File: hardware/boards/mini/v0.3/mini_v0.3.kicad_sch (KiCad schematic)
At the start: 96 parts, among them IC1 NAU88C22YG, IC3 IS42S16160J-6BLI, J1 Connector, J2 Top (A), J3 Bottom (B), U1 W25Q128JVP, U2 LTV-217-G, U4 STM32H750XBHx, Y1 Crystal_GND24, Y3 32.768kHz

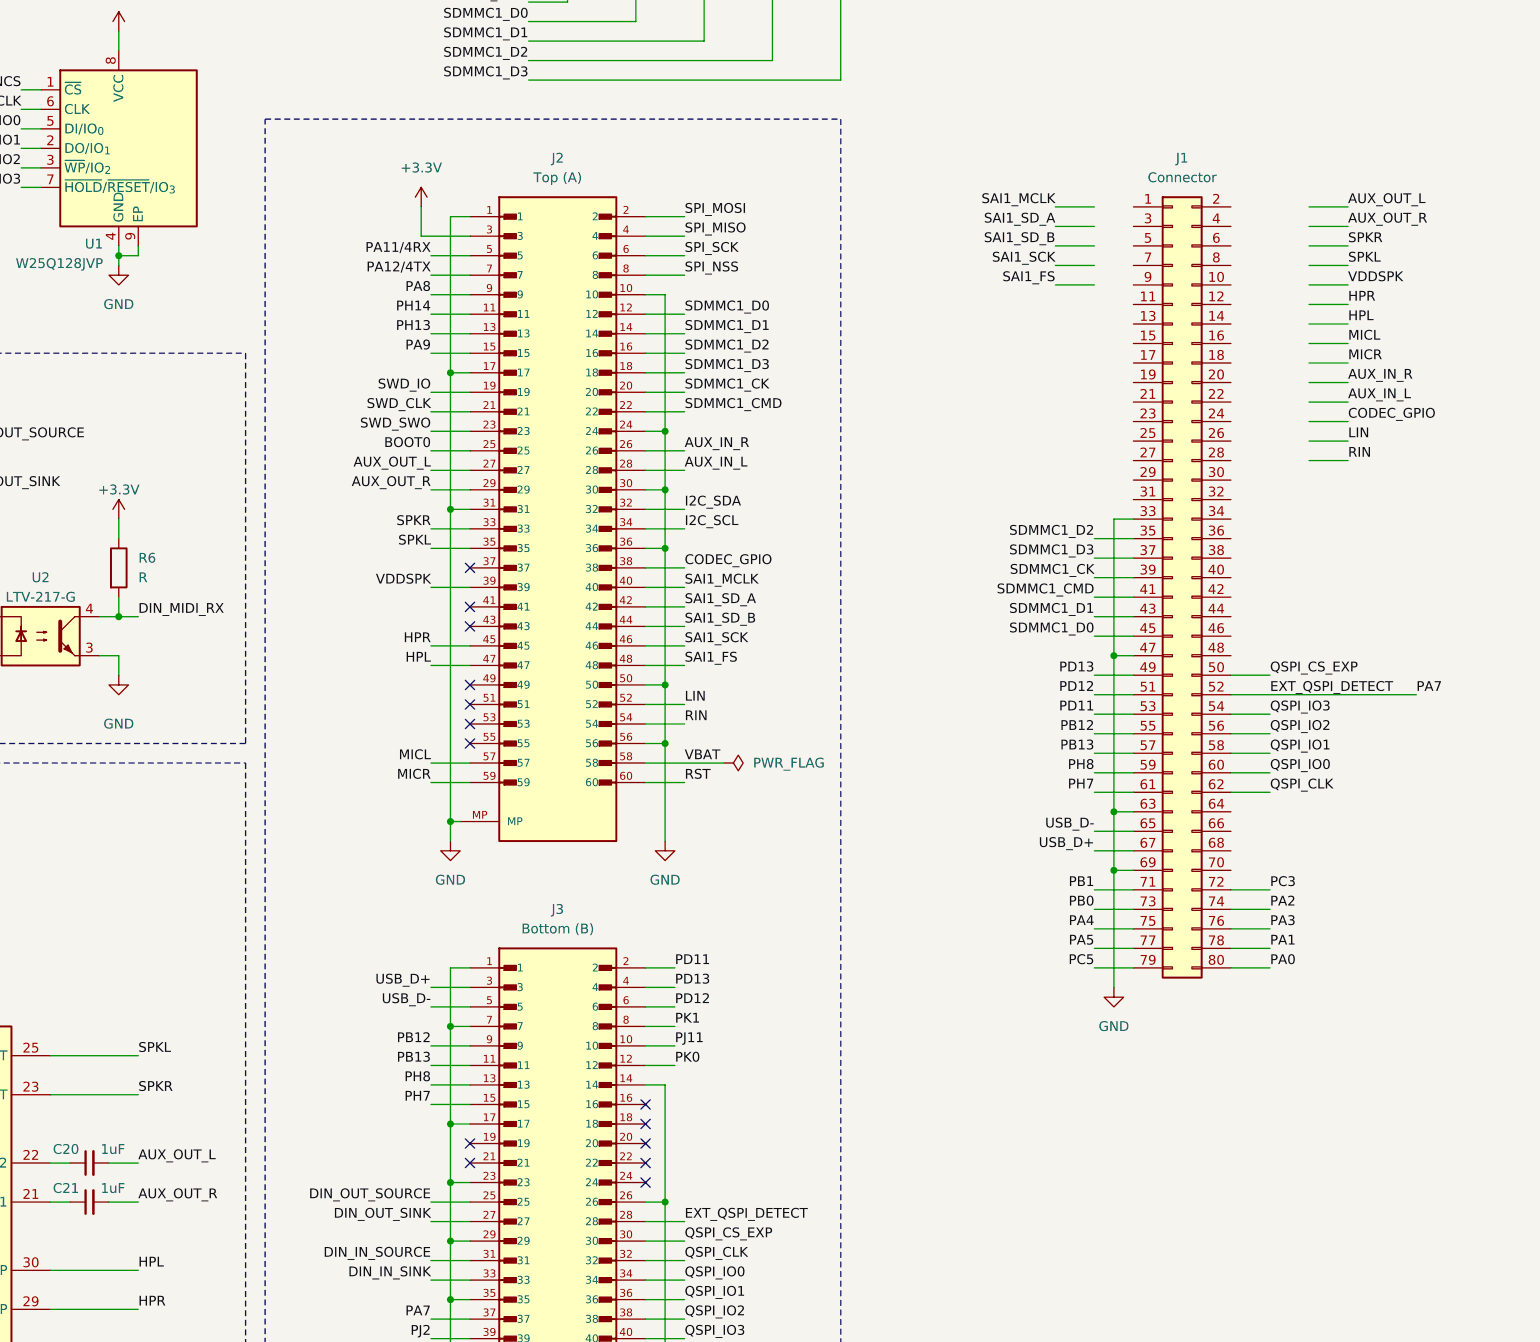
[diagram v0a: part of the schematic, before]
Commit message: mini: SWD, SPI, and audio codec layout
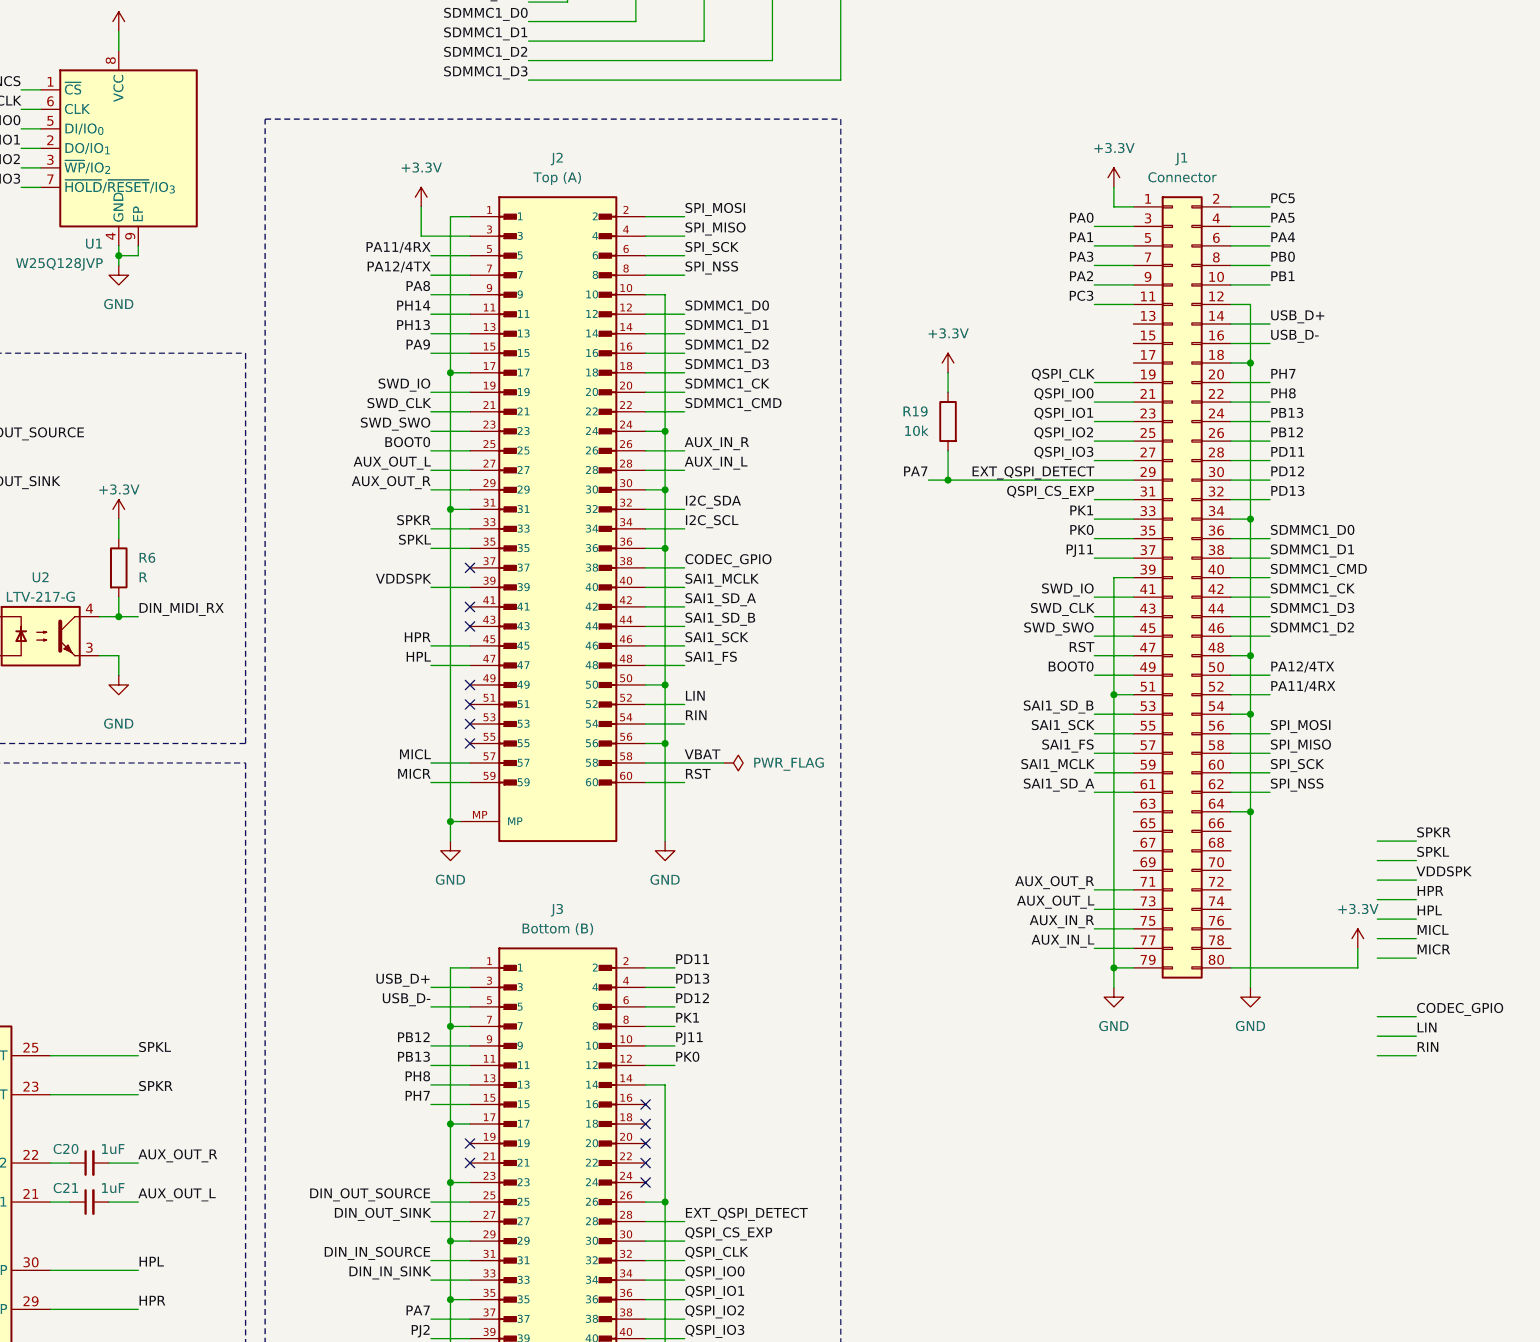
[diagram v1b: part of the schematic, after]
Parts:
- added R19: 10k, Resistor_SMD:R_0402_1005Metric, symbol Device:R
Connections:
- net +3.3V: now also J1.1 (Pin_1), J1.80 (Pin_80), R19.1
- net AUX_IN_L: now also J1.77 (Pin_77)
- net AUX_IN_R: now also J1.75 (Pin_75)
- net AUX_OUT_L: now also C21.2, J1.73 (Pin_73); no longer C20.2
- net AUX_OUT_R: now also C20.2, J1.71 (Pin_71); no longer C21.2
- net BOOT0: now also J1.49 (Pin_49)
- net EXT_QSPI_DETECT: now also J1.29 (Pin_29), R19.2; no longer J1.52 (Pin_52)
- net GND: now also J1.12 (Pin_12), J1.18 (Pin_18), J1.34 (Pin_34), J1.39 (Pin_39), J1.48 (Pin_48), J1.51 (Pin_51), J1.54 (Pin_54), J1.64 (Pin_64), J1.79 (Pin_79); no longer J1.33 (Pin_33), J1.47 (Pin_47), J1.63 (Pin_63), J1.69 (Pin_69)
- net PA0: now also J1.3 (Pin_3); no longer J1.80 (Pin_80)
- net PA1: now also J1.5 (Pin_5); no longer J1.78 (Pin_78)
- net PA11/4RX: now also J1.52 (Pin_52)
- net PA12/4TX: now also J1.50 (Pin_50)
- net PA2: now also J1.9 (Pin_9); no longer J1.74 (Pin_74)
- net PA3: now also J1.7 (Pin_7); no longer J1.76 (Pin_76)
- net PA4: now also J1.6 (Pin_6); no longer J1.75 (Pin_75)
- net PA5: now also J1.4 (Pin_4); no longer J1.77 (Pin_77)
- net PB0: now also J1.8 (Pin_8); no longer J1.73 (Pin_73)
- net PB1: now also J1.10 (Pin_10); no longer J1.71 (Pin_71)
- net PB12: now also J1.26 (Pin_26); no longer J1.55 (Pin_55)
- net PB13: now also J1.24 (Pin_24); no longer J1.57 (Pin_57)
- net PC3: now also J1.11 (Pin_11); no longer J1.72 (Pin_72)
- net PC5: now also J1.2 (Pin_2); no longer J1.79 (Pin_79)
- net PD11: now also J1.28 (Pin_28); no longer J1.53 (Pin_53)
- net PD12: now also J1.30 (Pin_30); no longer J1.51 (Pin_51)
- net PD13: now also J1.32 (Pin_32); no longer J1.49 (Pin_49)
- net PH7: now also J1.20 (Pin_20); no longer J1.61 (Pin_61)
- net PH8: now also J1.22 (Pin_22); no longer J1.59 (Pin_59)
- net PJ11: now also J1.37 (Pin_37)
- net PK0: now also J1.35 (Pin_35)
- net PK1: now also J1.33 (Pin_33)
- net QSPI_CLK: now also J1.19 (Pin_19); no longer J1.62 (Pin_62)
- net QSPI_CS_EXP: now also J1.31 (Pin_31); no longer J1.50 (Pin_50)
- net QSPI_IO0: now also J1.21 (Pin_21); no longer J1.60 (Pin_60)
- net QSPI_IO1: now also J1.23 (Pin_23); no longer J1.58 (Pin_58)
- net QSPI_IO2: now also J1.25 (Pin_25); no longer J1.56 (Pin_56)
- net QSPI_IO3: now also J1.27 (Pin_27); no longer J1.54 (Pin_54)
- net RST: now also J1.47 (Pin_47)
- net SAI1_FS: now also J1.57 (Pin_57)
- net SAI1_MCLK: now also J1.59 (Pin_59)
- net SAI1_SCK: now also J1.55 (Pin_55)
- net SAI1_SD_A: now also J1.61 (Pin_61)
- net SAI1_SD_B: now also J1.53 (Pin_53)
- net SDMMC1_CK: now also J1.42 (Pin_42); no longer J1.39 (Pin_39)
- net SDMMC1_CMD: now also J1.40 (Pin_40); no longer J1.41 (Pin_41)
- net SDMMC1_D0: now also J1.36 (Pin_36); no longer J1.45 (Pin_45)
- net SDMMC1_D1: now also J1.38 (Pin_38); no longer J1.43 (Pin_43)
- net SDMMC1_D2: now also J1.46 (Pin_46); no longer J1.35 (Pin_35)
- net SDMMC1_D3: now also J1.44 (Pin_44); no longer J1.37 (Pin_37)
- net SPI_MISO: now also J1.58 (Pin_58)
- net SPI_MOSI: now also J1.56 (Pin_56)
- net SPI_NSS: now also J1.62 (Pin_62)
- net SPI_SCK: now also J1.60 (Pin_60)
- net SWD_CLK: now also J1.43 (Pin_43)
- net SWD_IO: now also J1.41 (Pin_41)
- net SWD_SWO: now also J1.45 (Pin_45)
- net USB_D+: now also J1.14 (Pin_14); no longer J1.67 (Pin_67)
- net USB_D-: now also J1.16 (Pin_16); no longer J1.65 (Pin_65)
